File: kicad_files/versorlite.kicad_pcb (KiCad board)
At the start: 4 copper layers, 33 x 81.3 mm, 136 parts, among them J1 Conn_01x01_Socket, J10 IGN_2, J3 RFD900ux 10 Pin Header, J4 Conn_ARM_JTAG_SWD_10, J5 RFD900ux 3 Pin Power Select, J6 USB_C_Receptacle_USB2.0_16P, J7 Micro_SD_Card_Det2, J8 Conn_01x02_Socket, J9 IGN_1, Q1 FDMC510P-MS, Q2 AO3400A, Q3 AO3400A, SW1 SW_Push, SW2 SW_Push, U1 STM32F407VGTx, U10 W25Q128JVS, U11 LT1963AxST-3.3, U12 AP63205WU, U13 74LVC1G125, U2 MS5611-01BA, U3 BMI088, U4 MMC5983MA, U5 MAX-M10S, U6 BMP388, U7 LSM6DSM, U9 WE-TVS-82400102, Y1 LFXTAL036869Reel 8MHz Crystal

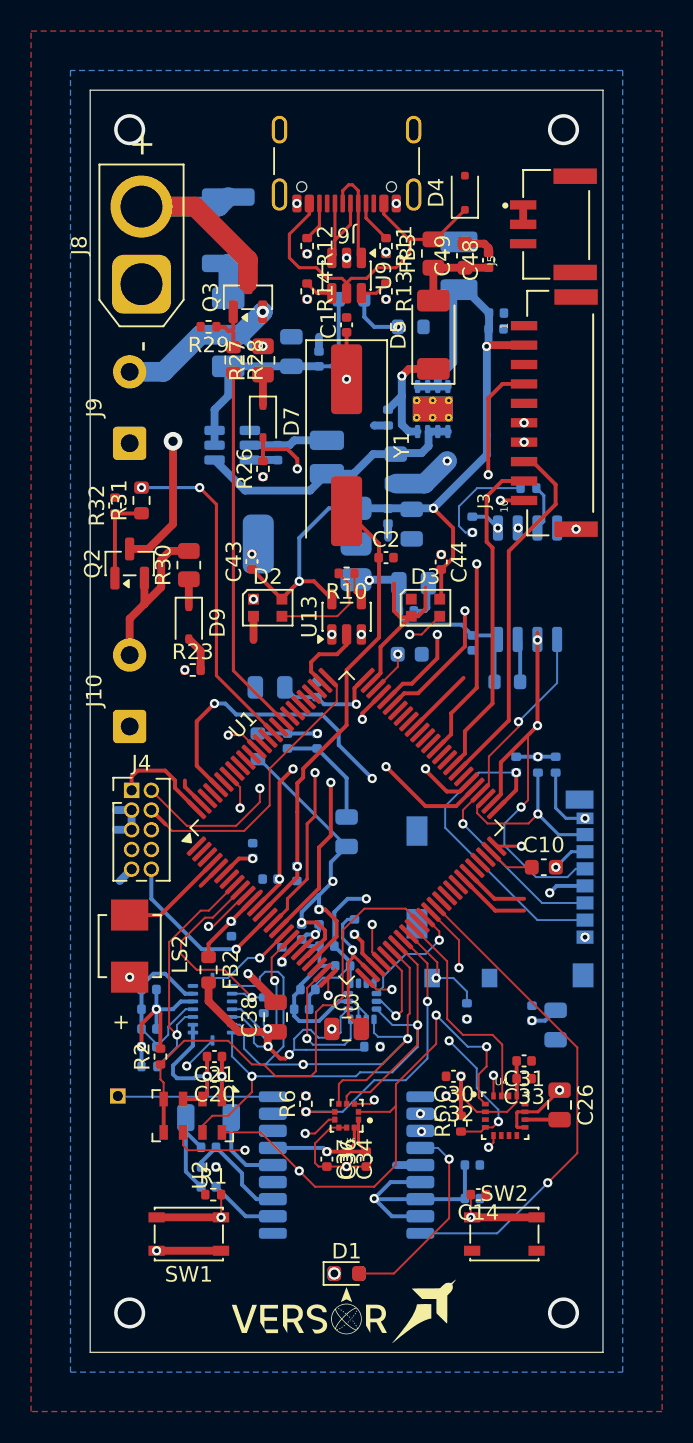
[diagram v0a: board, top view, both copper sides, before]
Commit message: Fix silkscreen readability
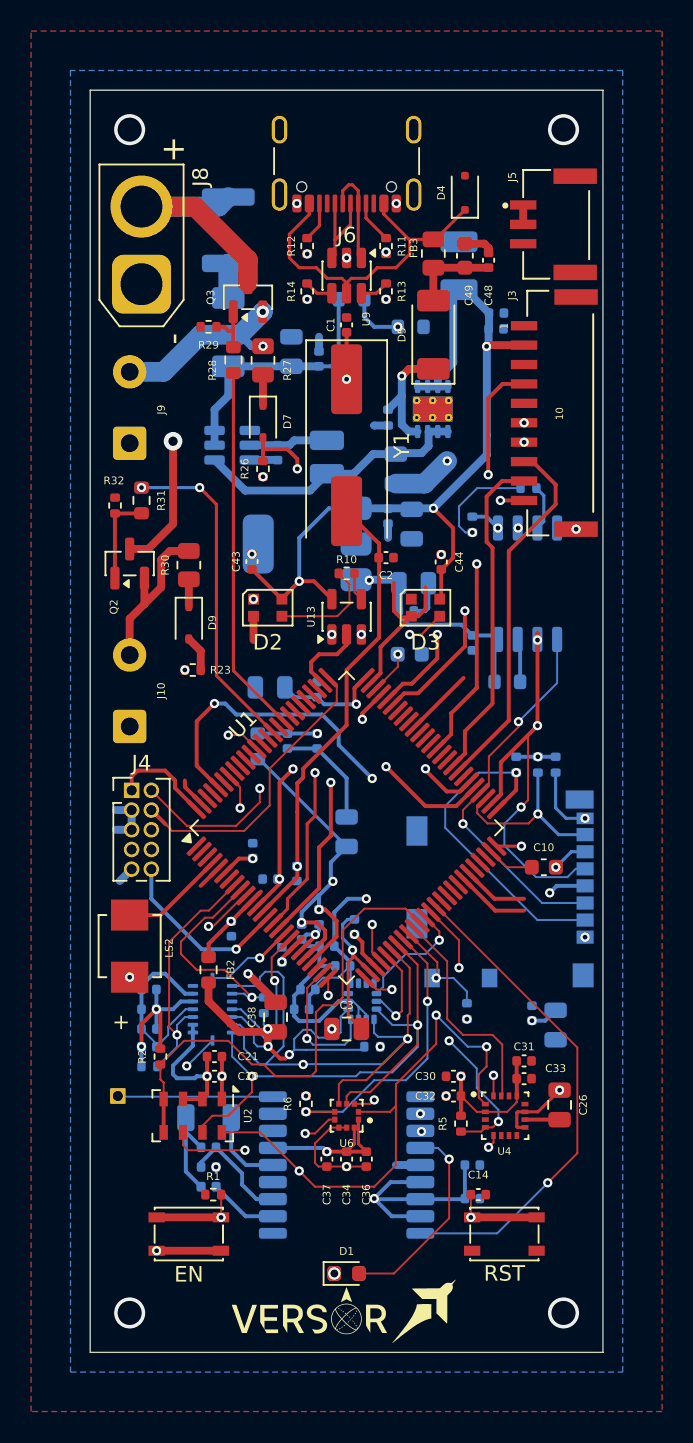
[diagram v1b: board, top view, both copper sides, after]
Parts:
- renumbered SW1 to EN, SW2 to RST

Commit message: impedance match u.fl line
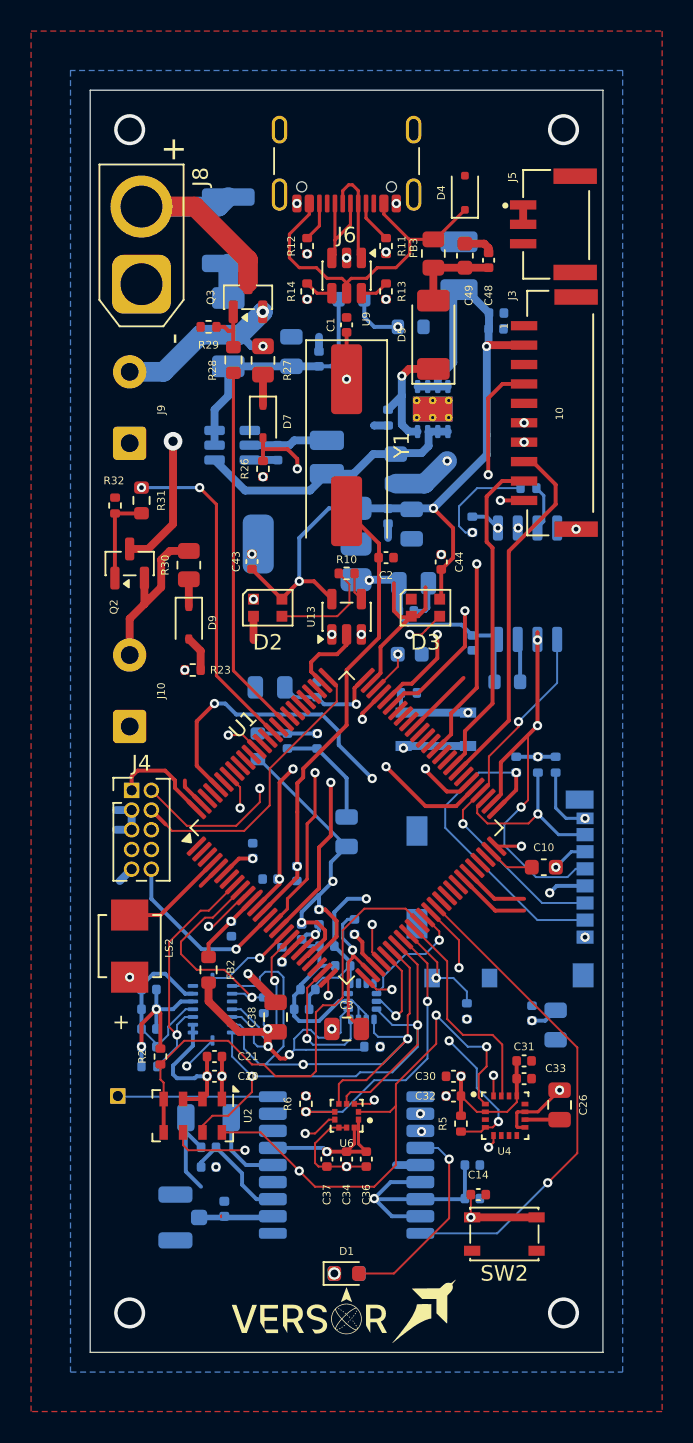
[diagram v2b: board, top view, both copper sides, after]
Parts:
- added J2: U.FL, Connector_Coaxial:U.FL_Hirose_U.FL-R-SMT-1_Vertical, B.Cu at (132.5, 134.8)
- R1: moved to B.Cu
- SW1: renamed from EN; moved to B.Cu
- moved SW1 36.2 mm to (149.3, 103.4), turned to 0 degrees
- moved R1 34.7 mm to (147.5, 101.0), turned to 180 degrees
- moved FB1 1.75 mm to (135.6, 134.3), turned to -90 degrees
- renumbered RST to SW2
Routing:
- net +3V3_MCU: track 73.1 -> 57.6 mm
- net Net-(U1-BOOT0): track 36.4 -> 25.2 mm

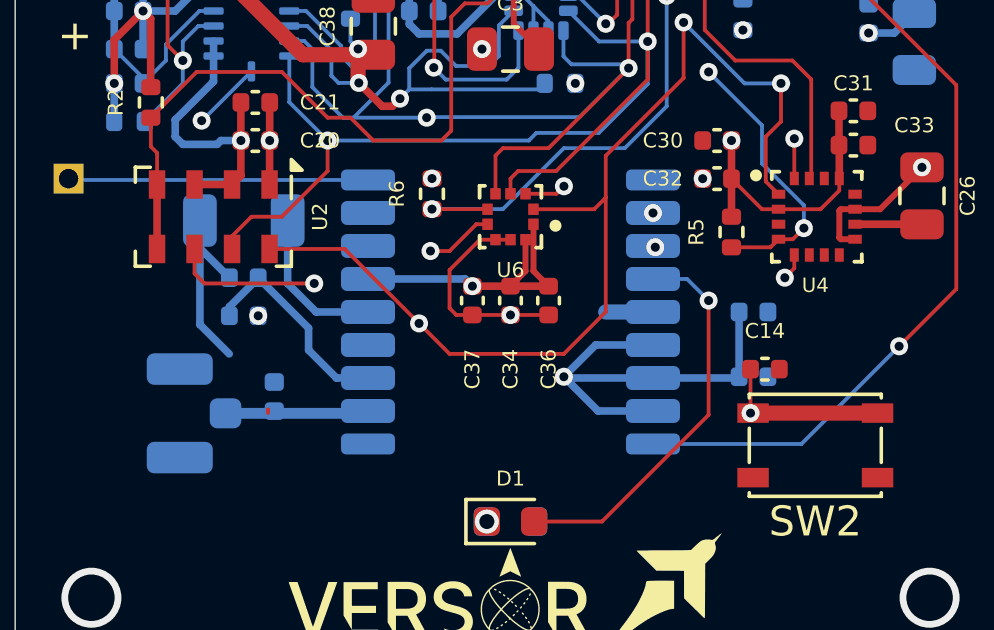
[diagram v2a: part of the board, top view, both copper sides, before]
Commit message: fix mcc, gps decaps
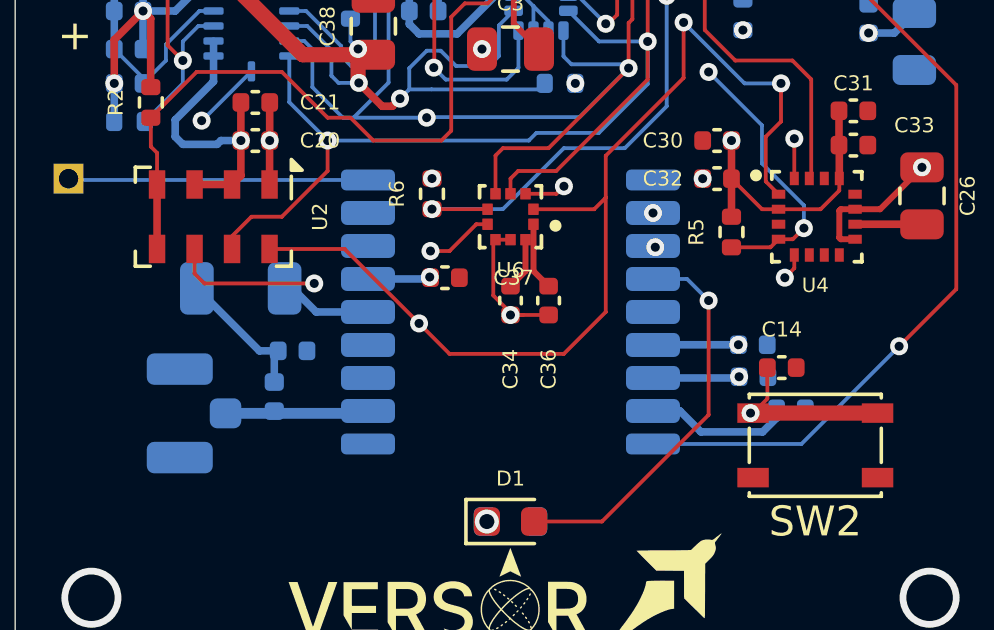
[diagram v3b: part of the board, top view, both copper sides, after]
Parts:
- moved C27 18.5 mm to (152.9, 134.7), turned to 180 degrees
- moved C35 2.93 mm to (136.2, 132.7)
- moved R7 2.26 mm to (134.5, 130.7)
- moved C37 1.19 mm to (141.3, 130.3), turned to 0 degrees
- moved C29 1.09 mm to (151.6, 132.5)
- moved C14 0.56 mm to (152.6, 133.3)
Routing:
- net GND: track 122.6 -> 111.6 mm
- net +3V3_SENSORS: track 90.9 -> 82.7 mm
- net Net-(U5-VCC_RF): track 5.17 -> 3.07 mm
- net Net-(C35-Pad2): track 6.24 -> 4.67 mm
- net /MCU/NRST: track 41.7 -> 42.5 mm

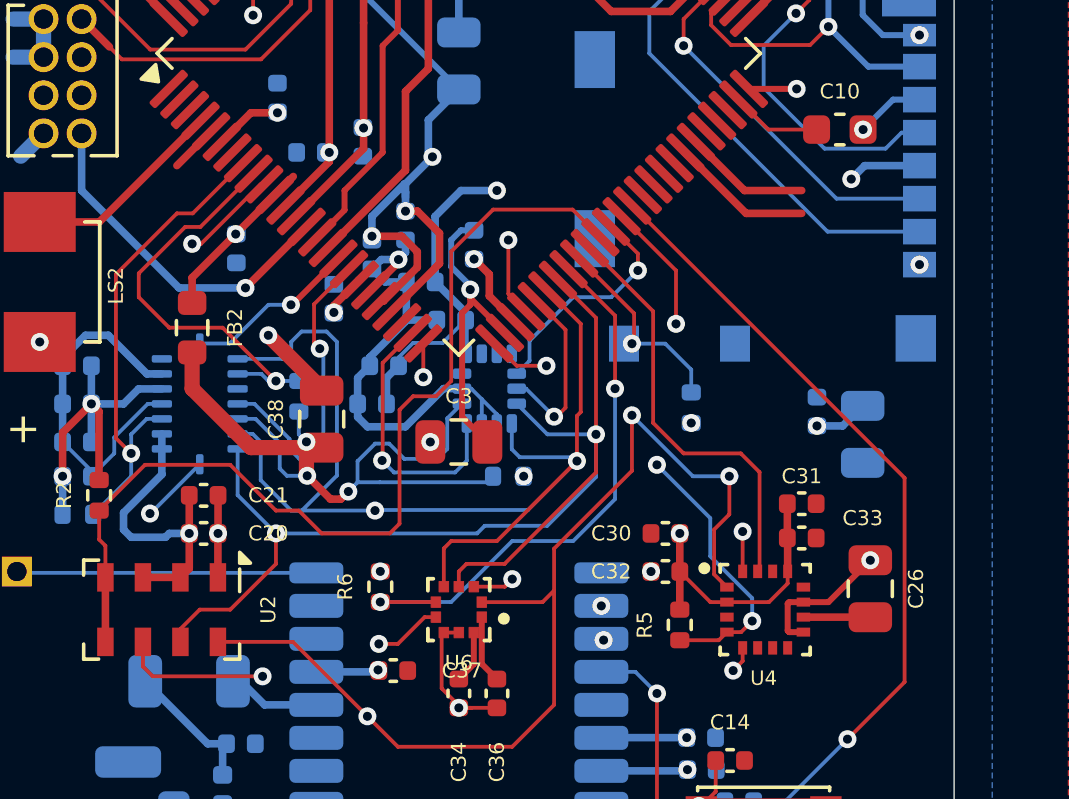
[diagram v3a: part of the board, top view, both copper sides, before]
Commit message: fix lsm decaps
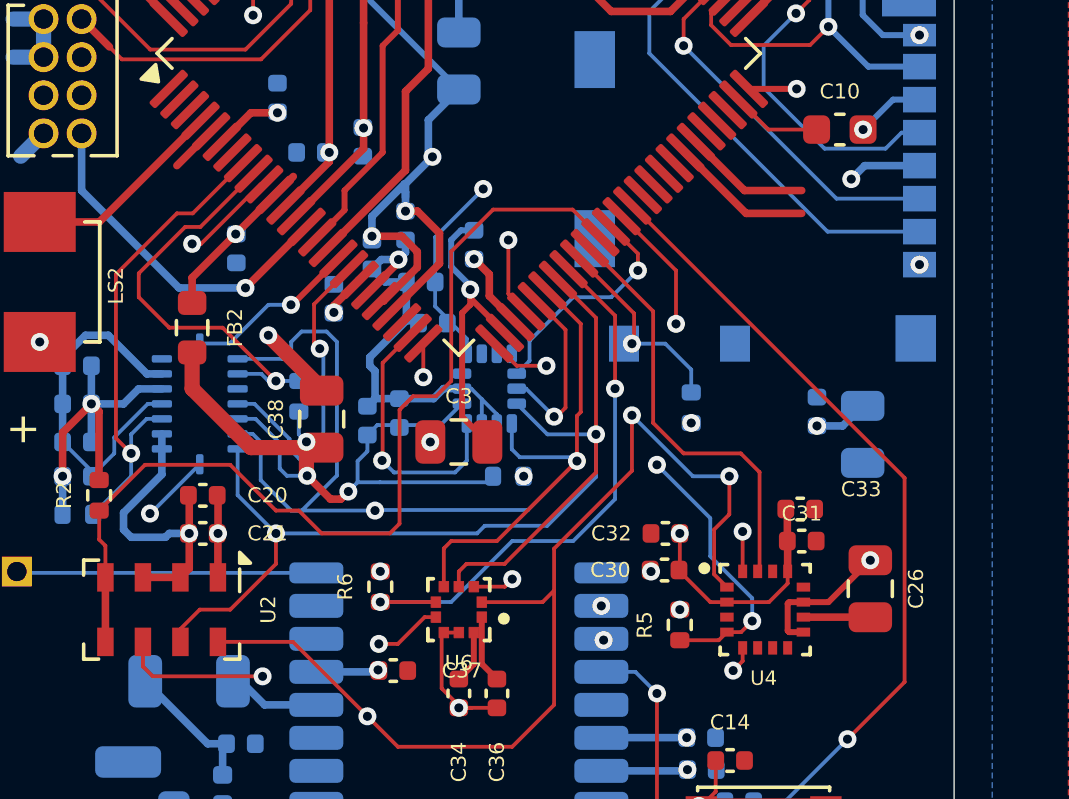
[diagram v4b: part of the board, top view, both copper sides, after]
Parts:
- moved C42 1.65 mm to (141.5, 121.7), turned to -90 degrees
- moved C20 1.27 mm to (135.0, 124.5)
- moved C21 1.27 mm to (135.0, 125.7)
- moved C32 1.27 mm to (150.4, 125.7)
- moved C31 1.24 mm to (154.9, 126.0)
- moved C30 1.22 mm to (150.4, 126.9)
- moved C33 0.97 mm to (154.9, 124.9)
- moved C40 0.62 mm to (142.6, 118.7)
- moved C41 0.58 mm to (140.5, 122.0), turned to -90 degrees
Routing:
- net +3V3_SENSORS: track 82.7 -> 74.9 mm, vias 12 -> 13
- net GND: track 111.6 -> 109.6 mm

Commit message: fix unconnected
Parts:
- removed C24: 1μf, Capacitor_SMD:C_0402_1005Metric
- removed C3: 10uf, Capacitor_SMD:C_0805_2012Metric
- moved C25 6.78 mm to (137.6, 123.9), turned to 90 degrees
- moved C18 2.03 mm to (143.5, 112.0), turned to 0 degrees
- moved R4 0.46 mm to (138.1, 120.7)
- moved R7 0.16 mm to (134.4, 130.6)
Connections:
- Q1 pad 1: /Power/+VBUS -> Net-(Q1-S)
- Q1 pad 3: +5V -> Net-(Q1-S)
- Q1 pad 4: (no net) -> /Power/+VBUS
- Q1 pad 5: (no net) -> +5V
- Q1 pad 6: (no net) -> +5V
- Q1 pad 7: (no net) -> +5V
- Q1 pad 8: (no net) -> +5V
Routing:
- net GND: track 109.6 -> 114.1 mm, vias 23 -> 25
- net +3V3_SENSORS: track 74.9 -> 71.1 mm, vias 13 -> 16
- net /MCU/USART3_TX_RADIO: track 35.1 -> 36.2 mm
- net +3V3_MCU: track 57.6 -> 56.8 mm
- net /MCU/CS_BARO_HIGH: track 32.4 -> 33.0 mm
- net /MCU/USART3_RX_RADIO: track 28.1 -> 27.6 mm

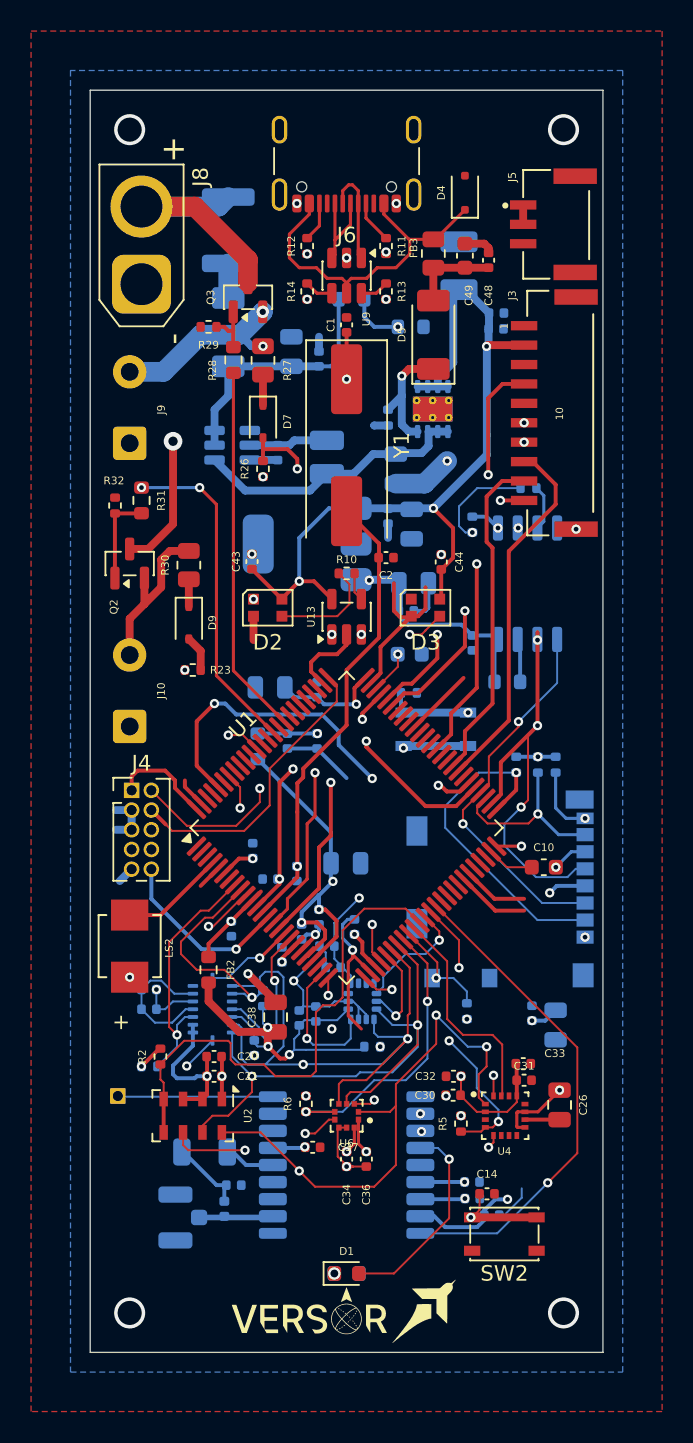
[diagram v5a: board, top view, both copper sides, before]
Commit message: Move switch back to front
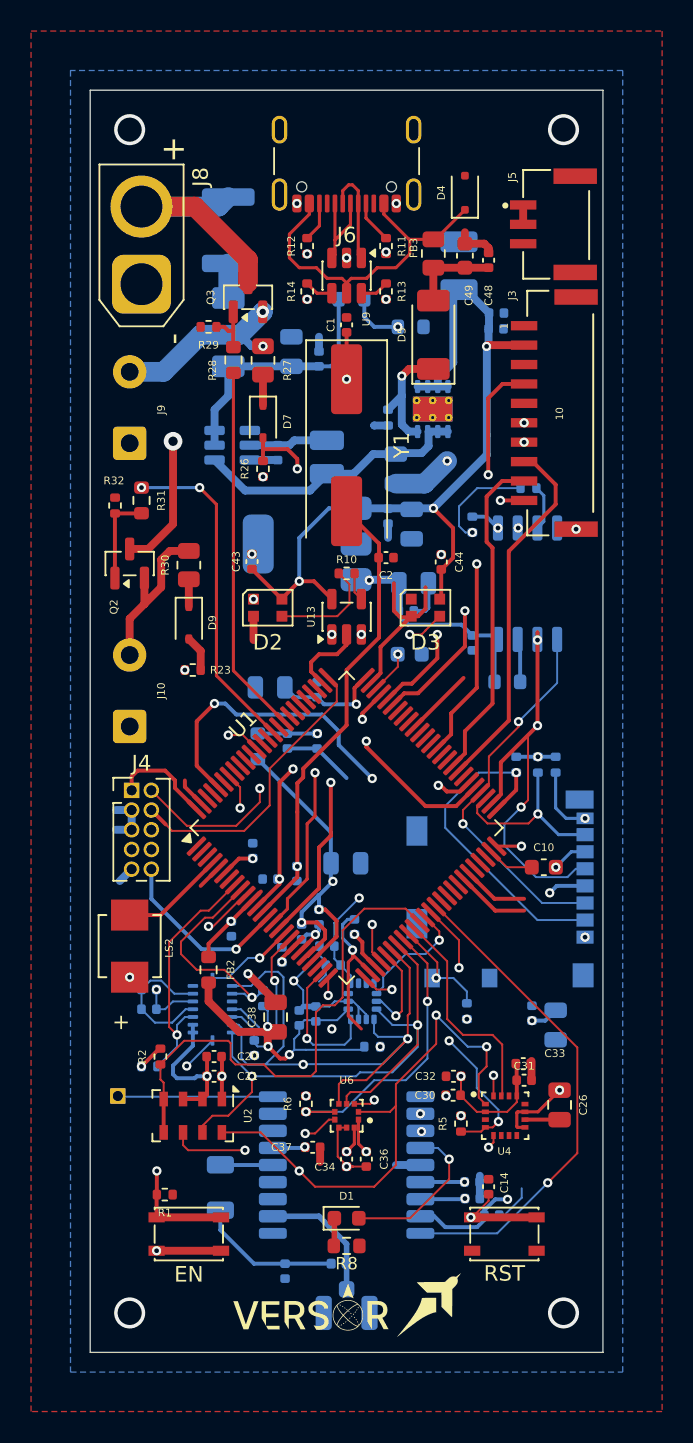
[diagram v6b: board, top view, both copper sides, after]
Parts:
- EN: renamed from SW1; moved to F.Cu
- R1, R8: moved to F.Cu
- moved EN 36.2 mm to (133.3, 135.9), turned to 180 degrees
- moved R1 35.9 mm to (131.8, 133.3)
- moved U.FL 12.6 mm to (143.5, 141.0), turned to -90 degrees
- moved FB1 8.17 mm to (143.0, 137.8), turned to 0 degrees
- moved C35 6.45 mm to (139.5, 138.3), turned to 90 degrees
- moved D1 3.56 mm to (143.5, 134.9)
- moved R7 2.50 mm to (135.4, 132.9), turned to -90 degrees
- moved R8 1.78 mm to (143.5, 136.7)
- moved G*** 0.52 mm to (148.9, 140.4)
- moved C14 0.47 mm to (152.7, 132.8), turned to -90 degrees
- moved G*** 0.26 mm to (141.2, 141.0)
- moved C40 0.15 mm to (142.6, 118.6)
- renumbered SW2 to RST, J2 to U.FL
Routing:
- net +3V3_MCU: track 56.8 -> 78.7 mm
- net Net-(U1-BOOT0): track 25.0 -> 35.8 mm
- net GND: track 114.1 -> 120.6 mm
- net /MCU/SPI1_SCK: track 65.1 -> 59.2 mm
- net Net-(C35-Pad2): track 4.67 -> 9.31 mm
- net Net-(J2-In): track 4.78 -> 8.41 mm
- net Net-(D1-A): track 13.3 -> 10.3 mm
- net Net-(D1-K): track 0.00 -> 1.79 mm, vias 1 -> 0
- net /MCU/EXTI0_BARO_LOW: track 38.9 -> 37.8 mm
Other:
- board text removed: "Versor Lite v0.1"
